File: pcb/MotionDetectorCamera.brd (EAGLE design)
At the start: 55.9 x 44.5 mm, 134 parts, among them J2 S-MOUNT-LENS-HOLDER, J3 MINI-USB-JACK, U1 LATTICE-ICE40HX4K-BG121, U10 NXP-NTB0102, U11 ON-NLAS3157, U12 ON-NLAS3157, U13 STM-STM32F730, U2 TI-TPS6280XYKAR, U22 TI-TPD4S012DRYR, U3 MICROSD-SOCKET, U4 TI-TPS6280XYKAR, U5 W989D6DBGX6I, U6 TI-TPS63805YFFR, U8 ON-AR0330CS1C12SPKA0, U9 TI-TMUX1574, X1 SITIME-SIT8021, X2 SITIME-SIT8021

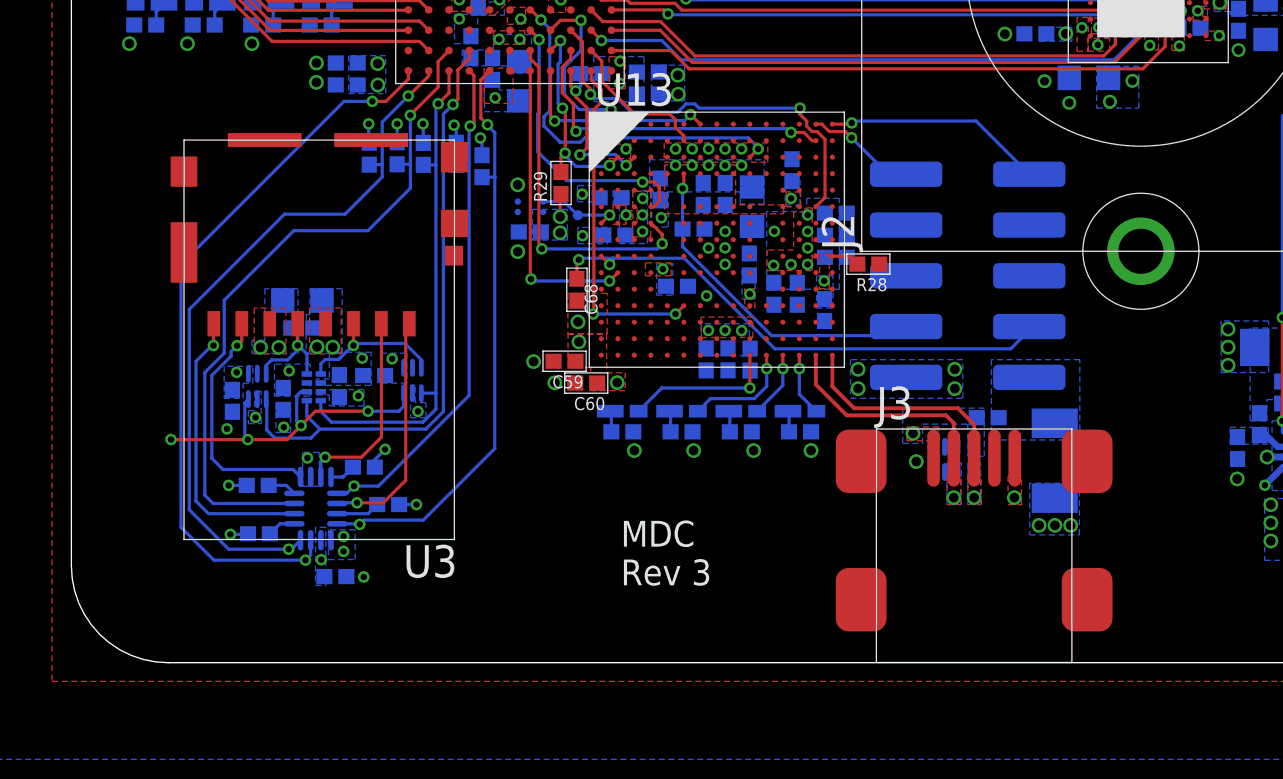
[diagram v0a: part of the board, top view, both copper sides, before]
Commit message: Add vias around ground pads
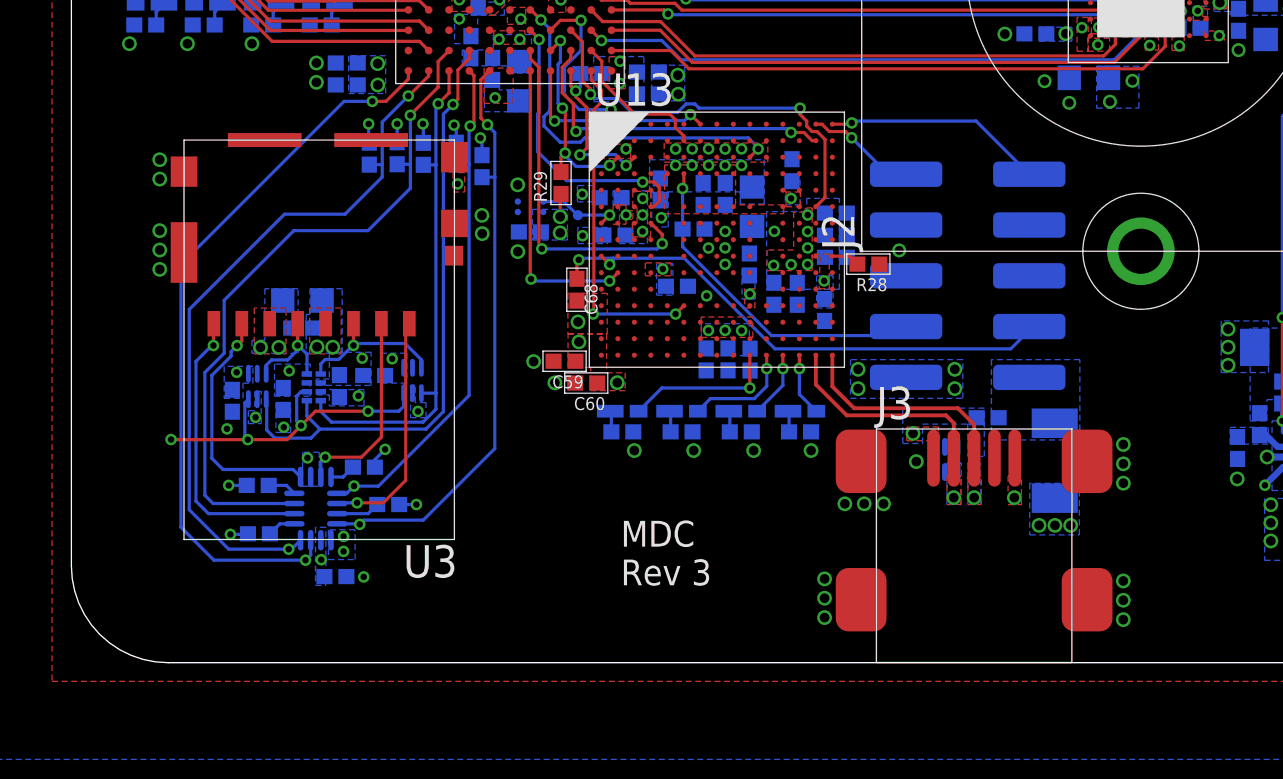
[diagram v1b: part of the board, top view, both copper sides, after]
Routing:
- net GND: vias 100 -> 121
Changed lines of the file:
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@@
 <layers>
 <layer number="1" name="Top" color="4" fill="1" visible="yes" active="yes"/>
-<layer number="2" name="Ground" color="16" fill="1" visible="no" active="yes"/>
+<layer number="2" name="Ground" color="16" fill="1" visible="yes" active="yes"/>
 <layer number="3" name="Route3" color="17" fill="1" visible="no" active="no"/>
 <layer number="4" name="Route4" color="18" fill="1" visible="no" active="no"/>
@@
 <layer number="13" name="Route13" color="21" fill="1" visible="no" active="no"/>
 <layer number="14" name="Route14" color="22" fill="1" visible="no" active="no"/>
-<layer number="15" name="Power" color="42" fill="1" visible="no" active="yes"/>
-<layer number="16" name="Bottom" color="1" fill="1" visible="no" active="yes"/>
+<layer number="15" name="Power" color="42" fill="1" visible="yes" active="yes"/>
+<layer number="16" name="Bottom" color="1" fill="1" visible="yes" active="yes"/>
 <layer number="17" name="Pads" color="2" fill="1" visible="yes" active="yes"/>
 <layer number="18" name="Vias" color="2" fill="1" visible="yes" active="yes"/>
@@
 <layer number="20" name="Dimension" color="24" fill="1" visible="yes" active="yes"/>
 <layer number="21" name="tPlace" color="7" fill="1" visible="yes" active="yes"/>
-<layer number="22" name="bPlace" color="7" fill="1" visible="no" active="yes"/>
+<layer number="22" name="bPlace" color="7" fill="1" visible="yes" active="yes"/>
 <layer number="23" name="tOrigins" color="15" fill="1" visible="yes" active="yes"/>
-<layer number="24" name="bOrigins" color="15" fill="1" visible="no" active="yes"/>
+<layer number="24" name="bOrigins" color="15" fill="1" visible="yes" active="yes"/>
 <layer number="25" name="tNames" color="7" fill="1" visible="yes" active="yes"/>
-<layer number="26" name="bNames" color="7" fill="1" visible="no" active="yes"/>
+<layer number="26" name="bNames" color="7" fill="1" visible="yes" active="yes"/>
 <layer number="27" name="tValues" color="7" fill="1" visible="yes" active="yes"/>
-<layer number="28" name="bValues" color="7" fill="1" visible="no" active="yes"/>
+<layer number="28" name="bValues" color="7" fill="1" visible="yes" active="yes"/>
 <layer number="29" name="tStop" color="7" fill="3" visible="yes" active="yes"/>
-<layer number="30" name="bStop" color="7" fill="6" visible="no" active="yes"/>
-<layer number="31" name="tCream" color="7" fill="4" visible="yes" active="yes"/>
+<layer number="30" name="bStop" color="7" fill="6" visible="yes" active="yes"/>
+<layer number="31" name="tCream" color="7" fill="4" visible="no" active="yes"/>
 <layer number="32" name="bCream" color="7" fill="5" visible="no" active="yes"/>
-<layer number="33" name="tFinish" color="6" fill="3" visible="yes" active="yes"/>
+<layer number="33" name="tFinish" color="6" fill="3" visible="no" active="yes"/>
 <layer number="34" name="bFinish" color="6" fill="6" visible="no" active="yes"/>
-<layer number="35" name="tGlue" color="7" fill="4" visible="yes" active="yes"/>
+<layer number="35" name="tGlue" color="7" fill="4" visible="no" active="yes"/>
 <layer number="36" name="bGlue" color="7" fill="5" visible="no" active="yes"/>
-<layer number="37" name="tTest" color="7" fill="1" visible="yes" active="yes"/>
+<layer number="37" name="tTest" color="7" fill="1" visible="no" active="yes"/>
 <layer number="38" name="bTest" color="7" fill="1" visible="no" active="yes"/>
 <layer number="39" name="tKeepout" color="4" fill="11" visible="no" active="yes"/>
 <layer number="40" name="bKeepout" color="1" fill="11" visible="no" active="yes"/>
 <layer number="41" name="tRestrict" color="4" fill="10" visible="yes" active="yes"/>
-<layer number="42" name="bRestrict" color="1" fill="10" visible="no" active="yes"/>
-<layer number="43" name="vRestrict" color="2" fill="10" visible="no" active="yes"/>
+<layer number="42" name="bRestrict" color="1" fill="10" visible="yes" active="yes"/>
+<layer number="43" name="vRestrict" color="2" fill="10" visible="yes" active="yes"/>
 <layer number="44" name="Drills" color="7" fill="1" visible="no" active="yes"/>
 <layer number="45" name="Holes" color="7" fill="1" visible="no" active="yes"/>
 <layer number="46" name="Milling" color="3" fill="1" visible="no" active="yes"/>
 <layer number="47" name="Measures" color="7" fill="1" visible="no" active="yes"/>
-<layer number="48" name="Document" color="7" fill="1" visible="no" active="yes"/>
+<layer number="48" name="Document" color="7" fill="1" visible="yes" active="yes"/>
 <layer number="49" name="Reference" color="7" fill="1" visible="no" active="yes"/>
 <layer number="50" name="dxf" color="7" fill="1" visible="no" active="no"/>
@@
 <via x="37.144959375" y="6.5024" extent="1-16" drill="0.381"/>
 <via x="33.281615625" y="7.9222625" extent="1-16" drill="0.381"/>
+<via x="41.437559375" y="8.595359375" extent="1-16" drill="0.381"/>
+<via x="41.437559375" y="7.833359375" extent="1-16" drill="0.381"/>
+<via x="41.437559375" y="7.071359375" extent="1-16" drill="0.381"/>
+<via x="41.43501875" y="3.22071875" extent="1-16" drill="0.381"/>
+<via x="41.43501875" y="2.45871875" extent="1-16" drill="0.381"/>
+<via x="41.43501875" y="1.69671875" extent="1-16" drill="0.381"/>
+<via x="29.6672" y="1.778" extent="1-16" drill="0.381"/>
+<via x="29.6672" y="2.54" extent="1-16" drill="0.381"/>
+<via x="29.6672" y="3.302" extent="1-16" drill="0.381"/>
+<via x="30.4673" y="6.2585625" extent="1-16" drill="0.381"/>
+<via x="31.2293" y="6.2585625" extent="1-16" drill="0.381"/>
+<via x="31.9913" y="6.2585625" extent="1-16" drill="0.381"/>
+<via x="3.4798" y="19.812" extent="1-16" drill="0.381"/>
+<via x="3.4798" y="19.05" extent="1-16" drill="0.381"/>
+<via x="3.4798" y="17.018" extent="1-16" drill="0.381"/>
+<via x="3.4798" y="16.256" extent="1-16" drill="0.381"/>
+<via x="3.4798" y="15.494" extent="1-16" drill="0.381"/>
+<via x="16.169640625" y="17.61998125" extent="1-16" drill="0.381"/>
+<via x="16.182340625" y="16.901159375" extent="1-16" drill="0.381"/>
+<via x="15.2146" y="18.8595" extent="1-16" drill="0.254"/>
+<polygon width="0.127" layer="1" thermals="no">
+<vertex x="15.034259375" y="19.304"/>
+<vertex x="15.034259375" y="18.542"/>
+<vertex x="15.494" y="18.542"/>
+<vertex x="15.494" y="19.304"/>
+</polygon>
+<via x="32.608521875" y="16.240759375" extent="1-16" drill="0.35"/>
 </signal>
 <signal name="ICE_PIX_CLK24MHZ">

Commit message: Cleaning up layout
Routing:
- net GND: vias 121 -> 125
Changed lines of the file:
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@@
 <layers>
 <layer number="1" name="Top" color="4" fill="1" visible="yes" active="yes"/>
-<layer number="2" name="Ground" color="16" fill="1" visible="yes" active="yes"/>
+<layer number="2" name="Ground" color="16" fill="1" visible="no" active="yes"/>
 <layer number="3" name="Route3" color="17" fill="1" visible="no" active="no"/>
 <layer number="4" name="Route4" color="18" fill="1" visible="no" active="no"/>
@@
 <layer number="13" name="Route13" color="21" fill="1" visible="no" active="no"/>
 <layer number="14" name="Route14" color="22" fill="1" visible="no" active="no"/>
-<layer number="15" name="Power" color="42" fill="1" visible="yes" active="yes"/>
-<layer number="16" name="Bottom" color="1" fill="1" visible="yes" active="yes"/>
+<layer number="15" name="Power" color="42" fill="1" visible="no" active="yes"/>
+<layer number="16" name="Bottom" color="1" fill="1" visible="no" active="yes"/>
 <layer number="17" name="Pads" color="2" fill="1" visible="yes" active="yes"/>
 <layer number="18" name="Vias" color="2" fill="1" visible="yes" active="yes"/>
@@
 <layer number="20" name="Dimension" color="24" fill="1" visible="yes" active="yes"/>
 <layer number="21" name="tPlace" color="7" fill="1" visible="yes" active="yes"/>
-<layer number="22" name="bPlace" color="7" fill="1" visible="yes" active="yes"/>
+<layer number="22" name="bPlace" color="7" fill="1" visible="no" active="yes"/>
 <layer number="23" name="tOrigins" color="15" fill="1" visible="yes" active="yes"/>
-<layer number="24" name="bOrigins" color="15" fill="1" visible="yes" active="yes"/>
+<layer number="24" name="bOrigins" color="15" fill="1" visible="no" active="yes"/>
 <layer number="25" name="tNames" color="7" fill="1" visible="yes" active="yes"/>
-<layer number="26" name="bNames" color="7" fill="1" visible="yes" active="yes"/>
+<layer number="26" name="bNames" color="7" fill="1" visible="no" active="yes"/>
 <layer number="27" name="tValues" color="7" fill="1" visible="yes" active="yes"/>
-<layer number="28" name="bValues" color="7" fill="1" visible="yes" active="yes"/>
+<layer number="28" name="bValues" color="7" fill="1" visible="no" active="yes"/>
 <layer number="29" name="tStop" color="7" fill="3" visible="yes" active="yes"/>
-<layer number="30" name="bStop" color="7" fill="6" visible="yes" active="yes"/>
-<layer number="31" name="tCream" color="7" fill="4" visible="no" active="yes"/>
+<layer number="30" name="bStop" color="7" fill="6" visible="no" active="yes"/>
+<layer number="31" name="tCream" color="7" fill="4" visible="yes" active="yes"/>
 <layer number="32" name="bCream" color="7" fill="5" visible="no" active="yes"/>
-<layer number="33" name="tFinish" color="6" fill="3" visible="no" active="yes"/>
+<layer number="33" name="tFinish" color="6" fill="3" visible="yes" active="yes"/>
 <layer number="34" name="bFinish" color="6" fill="6" visible="no" active="yes"/>
-<layer number="35" name="tGlue" color="7" fill="4" visible="no" active="yes"/>
+<layer number="35" name="tGlue" color="7" fill="4" visible="yes" active="yes"/>
 <layer number="36" name="bGlue" color="7" fill="5" visible="no" active="yes"/>
-<layer number="37" name="tTest" color="7" fill="1" visible="no" active="yes"/>
+<layer number="37" name="tTest" color="7" fill="1" visible="yes" active="yes"/>
 <layer number="38" name="bTest" color="7" fill="1" visible="no" active="yes"/>
 <layer number="39" name="tKeepout" color="4" fill="11" visible="no" active="yes"/>
 <layer number="40" name="bKeepout" color="1" fill="11" visible="no" active="yes"/>
 <layer number="41" name="tRestrict" color="4" fill="10" visible="yes" active="yes"/>
-<layer number="42" name="bRestrict" color="1" fill="10" visible="yes" active="yes"/>
-<layer number="43" name="vRestrict" color="2" fill="10" visible="yes" active="yes"/>
+<layer number="42" name="bRestrict" color="1" fill="10" visible="no" active="yes"/>
+<layer number="43" name="vRestrict" color="2" fill="10" visible="no" active="yes"/>
 <layer number="44" name="Drills" color="7" fill="1" visible="no" active="yes"/>
 <layer number="45" name="Holes" color="7" fill="1" visible="no" active="yes"/>
 <layer number="46" name="Milling" color="3" fill="1" visible="no" active="yes"/>
 <layer number="47" name="Measures" color="7" fill="1" visible="no" active="yes"/>
-<layer number="48" name="Document" color="7" fill="1" visible="yes" active="yes"/>
+<layer number="48" name="Document" color="7" fill="1" visible="no" active="yes"/>
 <layer number="49" name="Reference" color="7" fill="1" visible="no" active="yes"/>
 <layer number="50" name="dxf" color="7" fill="1" visible="no" active="no"/>
@@
 <vertex x="27.404059375" y="16.256"/>
 <vertex x="27.404059375" y="15.445740625"/>
-<vertex x="29.182059375" y="15.445740625"/>
-<vertex x="29.182059375" y="17.91461875"/>
+<vertex x="29.202378125" y="15.445740625"/>
+<vertex x="29.202378125" y="17.91461875"/>
 <vertex x="28.9052" y="17.91461875"/>
 <vertex x="28.9052" y="17.74951875"/>
@@
 </polygon>
 <polygon width="0.127" layer="1" thermals="no">
-<vertex x="23.368" y="19.6088"/>
-<vertex x="23.368" y="17.683478125"/>
-<vertex x="28.05938125" y="17.683478125"/>
-<vertex x="28.05938125" y="18.034"/>
-<vertex x="26.162" y="18.034"/>
-<vertex x="26.162" y="19.6088"/>
+<vertex x="23.114" y="19.6088"/>
+<vertex x="23.114" y="16.413475"/>
+<vertex x="27.9679375" y="16.413475"/>
+<vertex x="27.9679375" y="19.6088"/>
 </polygon>
 <polygon width="0.127" layer="16" thermals="no">
@@
 </polygon>
 <via x="32.608521875" y="16.240759375" extent="1-16" drill="0.35"/>
+<via x="22.49931875" y="14.386559375" extent="1-16" drill="0.254"/>
+<polygon width="0.127" layer="1" thermals="no">
+<vertex x="22.9489" y="14.815815625"/>
+<vertex x="22.098" y="14.815815625"/>
+<vertex x="22.098" y="13.97"/>
+<vertex x="22.9489" y="13.97"/>
+</polygon>
+<via x="27.6606" y="18.321021875" extent="1-16" drill="0.254"/>
+<via x="27.6733" y="18.9103" extent="1-16" drill="0.254"/>
+<via x="27.67838125" y="17.655540625" extent="1-16" drill="0.254"/>
 </signal>
 <signal name="ICE_PIX_CLK24MHZ">
@@
 <via x="29.6519625" y="15.039340625" extent="1-16" drill="0.254" diameter="0.254"/>
 <polygon width="0.127" layer="1" thermals="no">
-<vertex x="29.184603125" y="16.0909"/>
-<vertex x="29.184603125" y="15.971521875"/>
+<vertex x="29.286203125" y="16.0909"/>
+<vertex x="29.286203125" y="15.971521875"/>
 <vertex x="29.488384375" y="15.971521875"/>
 <vertex x="29.4574" y="14.732"/>

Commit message: Layout progress
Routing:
- net GND: vias 125 -> 129

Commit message: Layout progress
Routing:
- net GND: vias 129 -> 138
- net 1V8: vias 71 -> 73
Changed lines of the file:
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@@
 <vertex x="27.386278125" y="17.7677375"/>
 <vertex x="27.386278125" y="14.709140625"/>
-<vertex x="30.248859375" y="14.709140625"/>
-<vertex x="30.248859375" y="18.288"/>
+<vertex x="30.020259375" y="14.709140625"/>
+<vertex x="30.020259375" y="18.288"/>
 <vertex x="28.966159375" y="18.288"/>
 <vertex x="28.966159375" y="17.77564375"/>
@@
 <via x="12.133578125" y="33.167321875" extent="1-16" drill="0.381"/>
 <polygon width="0.127" layer="16" thermals="no">
-<vertex x="6.468109375" y="36.440109375"/>
-<vertex x="8.1318125" y="34.7764125"/>
-<vertex x="9.5415125" y="36.1861125"/>
-<vertex x="7.877809375" y="37.849809375"/>
+<vertex x="6.222996875" y="36.194996875"/>
+<vertex x="7.8867" y="34.5313"/>
+<vertex x="9.914890625" y="36.559490625"/>
+<vertex x="8.2511875" y="38.2231875"/>
 </polygon>
 <polygon width="0.127" layer="16" thermals="no">
@@
 <vertex x="40.7162" y="25.4"/>
 </polygon>
+<via x="9.568178125" y="36.60648125" extent="1-16" drill="0.254"/>
+<via x="7.820659375" y="34.884359375" extent="1-16" drill="0.254"/>
 </signal>
 <signal name="GND">
@@
 <via x="23.90648125" y="22.3926375" extent="1-16" drill="0.381"/>
 <via x="23.581359375" y="29.49448125" extent="1-16" drill="0.254"/>
-<via x="24.3713" y="30.700978125" extent="1-16" drill="0.381"/>
+<via x="24.3713" y="30.446978125" extent="1-16" drill="0.381"/>
 <via x="23.876" y="32.3088" extent="1-16" drill="0.381"/>
 <via x="23.876" y="33.235896875" extent="1-16" drill="0.381"/>
@@
 </polygon>
 <polygon width="0.127" layer="16" thermals="no">
-<vertex x="5.452109375" y="37.710109375"/>
-<vertex x="6.39318125" y="36.769040625"/>
+<vertex x="4.827271875" y="37.085271875"/>
+<vertex x="5.76834375" y="36.144203125"/>
 <vertex x="7.716521875" y="38.09238125"/>
 <vertex x="6.77545" y="39.03345"/>
@@
 <via x="11.02868125" y="34.376359375" extent="1-16" drill="0.381"/>
 <polygon width="0.127" layer="16" thermals="no">
-<vertex x="8.44041875" y="34.7218"/>
-<vertex x="10.12698125" y="33.035240625"/>
-<vertex x="11.450321875" y="34.35858125"/>
-<vertex x="9.763759375" y="36.045140625"/>
+<vertex x="8.060690625" y="34.342071875"/>
+<vertex x="9.747253125" y="32.6555125"/>
+<vertex x="11.77798125" y="34.686240625"/>
+<vertex x="10.09141875" y="36.3728"/>
 </polygon>
 <via x="5.184140625" y="37.07638125" extent="1-16" drill="0.381" diameter="0.254"/>
@@
 <vertex x="30.48" y="21.719540625"/>
 </polygon>
+<via x="27.6987" y="20.233640625" extent="1-16" drill="0.254"/>
+<via x="24.3713" y="31.208978125" extent="1-16" drill="0.381"/>
+<via x="20.8026" y="38.851840625" extent="1-16" drill="0.381"/>
+<via x="20.8026" y="38.1127" extent="1-16" drill="0.381"/>
+<via x="24.239221875" y="11.460478125" extent="1-16" drill="0.381"/>
+<via x="8.376921875" y="34.31031875" extent="1-16" drill="0.254"/>
+<via x="10.132059375" y="36.065459375" extent="1-16" drill="0.254"/>
+<via x="30.939740625" y="18.458178125" extent="1-16" drill="0.381"/>
+<via x="30.866078125" y="14.91488125" extent="1-16" drill="0.381"/>
 </signal>
 <signal name="ICE_PIX_CLK24MHZ">

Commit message: Layout progress
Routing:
- net GND: vias 138 -> 140
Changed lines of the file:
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@@
 <contactref element="U8" pad="C4"/>
 <wire x1="41.443" y1="29.2498" x2="41.4528" y2="29.2596" width="0.2032" layer="1"/>
-<via x="41.4528" y="29.778959375" extent="1-16" drill="0.381"/>
+<via x="41.0972" y="29.778959375" extent="1-16" drill="0.381"/>
 <via x="42.418" y="28.2702" extent="1-16" drill="0.254"/>
 <contactref element="U8" pad="B7"/>
@@
 <via x="30.939740625" y="18.458178125" extent="1-16" drill="0.381"/>
 <via x="30.866078125" y="14.91488125" extent="1-16" drill="0.381"/>
+<via x="46.47691875" y="27.406596875" extent="1-16" drill="0.381"/>
+<via x="41.8592" y="29.778959375" extent="1-16" drill="0.381"/>
 </signal>
 <signal name="ICE_PIX_CLK24MHZ">
@@
 <polygon width="0.127" layer="1" thermals="no">
 <vertex x="14.986" y="26.278840625"/>
-<vertex x="14.986" y="25.654"/>
-<vertex x="15.748" y="25.654"/>
+<vertex x="14.986" y="25.16631875"/>
+<vertex x="15.748" y="25.16631875"/>
 <vertex x="15.748" y="26.278840625"/>
 </polygon>

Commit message: Layout progress
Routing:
- net ICE_SD_DAT3: track 20.2 -> 27.6 mm
- net ICE_SD_DAT2: track 23.2 -> 27.9 mm
- net ICE_SD_DAT1: track 27.4 -> 28.1 mm
